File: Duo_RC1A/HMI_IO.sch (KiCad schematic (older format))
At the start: 57 parts, among them P3 CONN_2_SMD_BACKLIGHT, P4 CONN_2_SMD_BACKLIGHT, P5 PIN_ARRAY_4X1

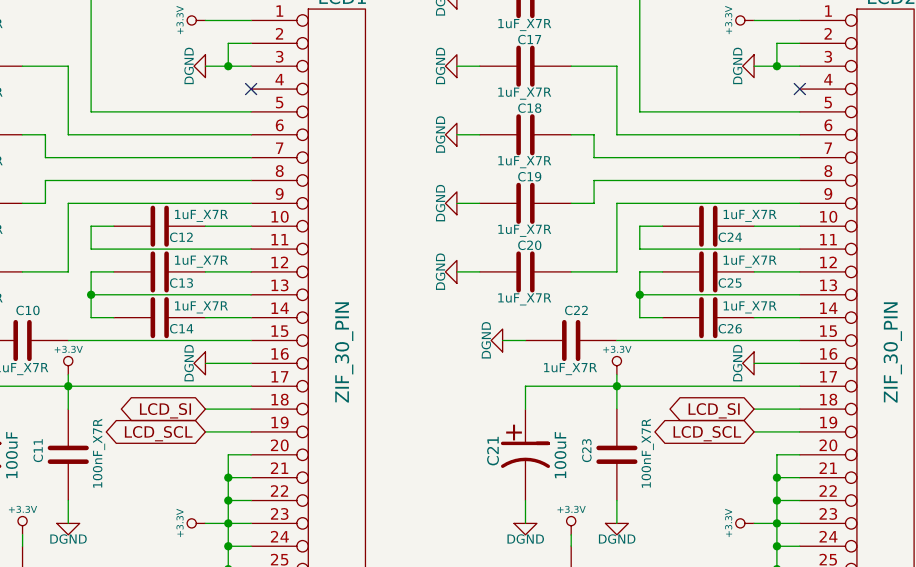
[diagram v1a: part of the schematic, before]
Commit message: Working on the BottomBoard layout. Moved the ITEAD Coreboard to the board left side so there is more space for the linear regulators. Stopped on the USB OTG and USB Host layout.
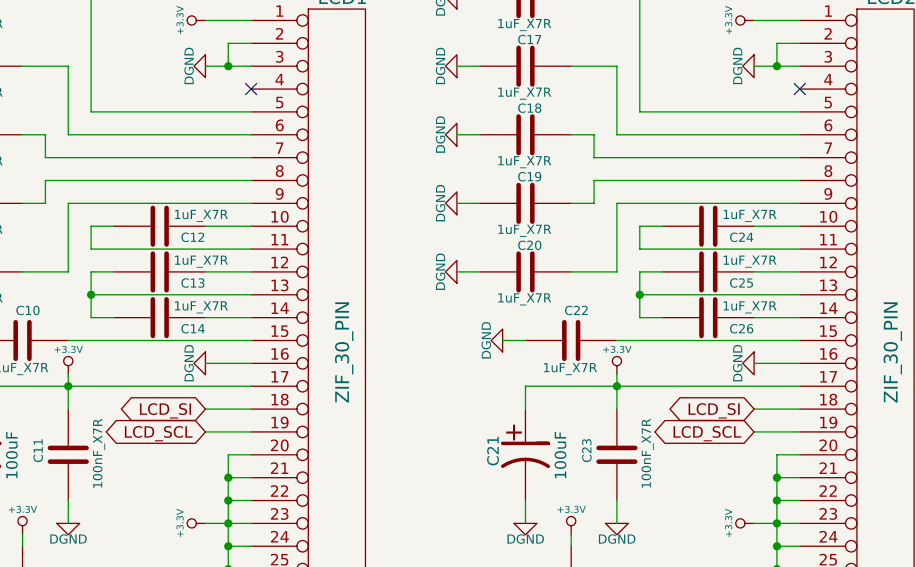
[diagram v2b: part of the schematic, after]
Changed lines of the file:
@@
 U 1 1 5371B976
 P 4900 3050
-F 0 "C26" V 4950 2900 40  0000 L CNN
+F 0 "C26" V 4950 2850 40  0000 L CNN
 F 1 "1uF_X7R" V 4850 2750 40  0000 L CNN
 F 2 "Duo_Audio_HMI_RC1A:SM0603" H 4938 2900 30  0001 C CNN
@@
 U 1 1 5371C10E
 P 4900 2850
-F 0 "C25" V 4950 2700 40  0000 L CNN
+F 0 "C25" V 4950 2650 40  0000 L CNN
 F 1 "1uF_X7R" V 4850 2550 40  0000 L CNN
 F 2 "Duo_Audio_HMI_RC1A:SM0603" H 4938 2700 30  0001 C CNN
@@
 U 1 1 5371CD0F
 P 4900 2650
-F 0 "C24" V 4950 2500 40  0000 L CNN
+F 0 "C24" V 4950 2450 40  0000 L CNN
 F 1 "1uF_X7R" V 4850 2350 40  0000 L CNN
 F 2 "Duo_Audio_HMI_RC1A:SM0603" H 4938 2500 30  0001 C CNN
@@
 U 1 1 53729A09
 P 2500 3050
-F 0 "C14" V 2550 2900 40  0000 L CNN
+F 0 "C14" V 2550 2850 40  0000 L CNN
 F 1 "1uF_X7R" V 2450 2750 40  0000 L CNN
 F 2 "Duo_Audio_HMI_RC1A:SM0603" H 2538 2900 30  0001 C CNN
@@
 U 1 1 53729A0F
 P 2500 2850
-F 0 "C13" V 2550 2700 40  0000 L CNN
+F 0 "C13" V 2550 2650 40  0000 L CNN
 F 1 "1uF_X7R" V 2450 2550 40  0000 L CNN
 F 2 "Duo_Audio_HMI_RC1A:SM0603" H 2538 2700 30  0001 C CNN
@@
 U 1 1 53729A2E
 P 2500 2650
-F 0 "C12" V 2550 2500 40  0000 L CNN
+F 0 "C12" V 2550 2450 40  0000 L CNN
 F 1 "1uF_X7R" V 2450 2350 40  0000 L CNN
 F 2 "Duo_Audio_HMI_RC1A:SM0603" H 2538 2500 30  0001 C CNN

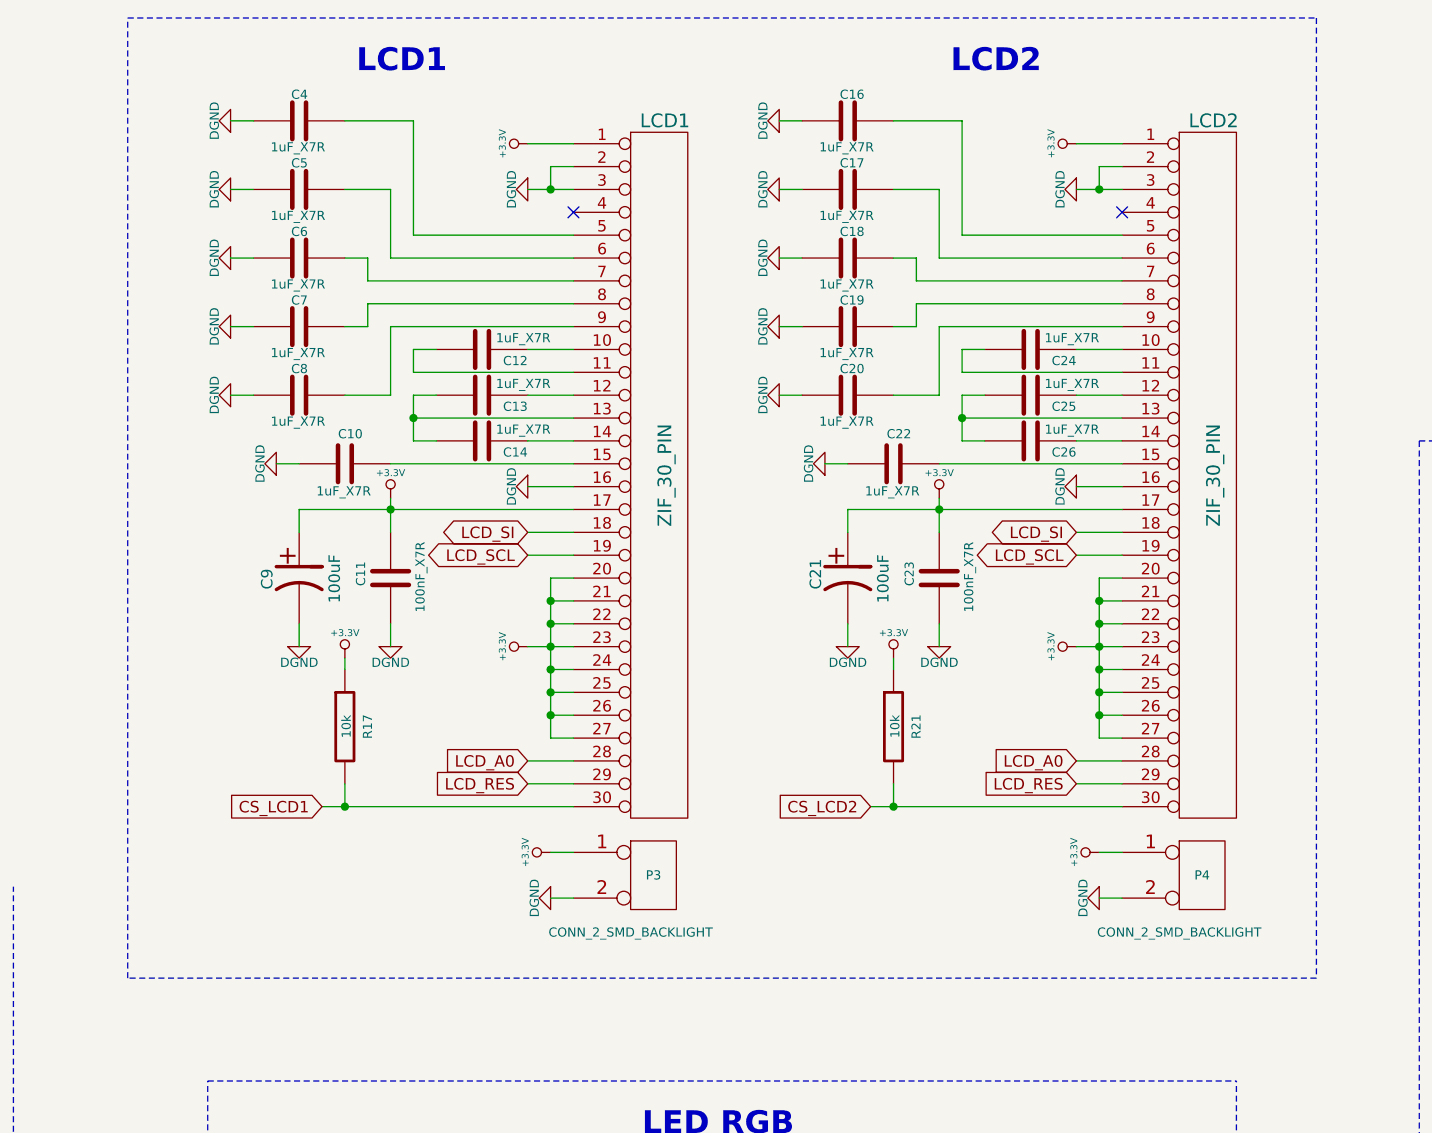
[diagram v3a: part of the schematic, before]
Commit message: Finished the TopBoard layout.
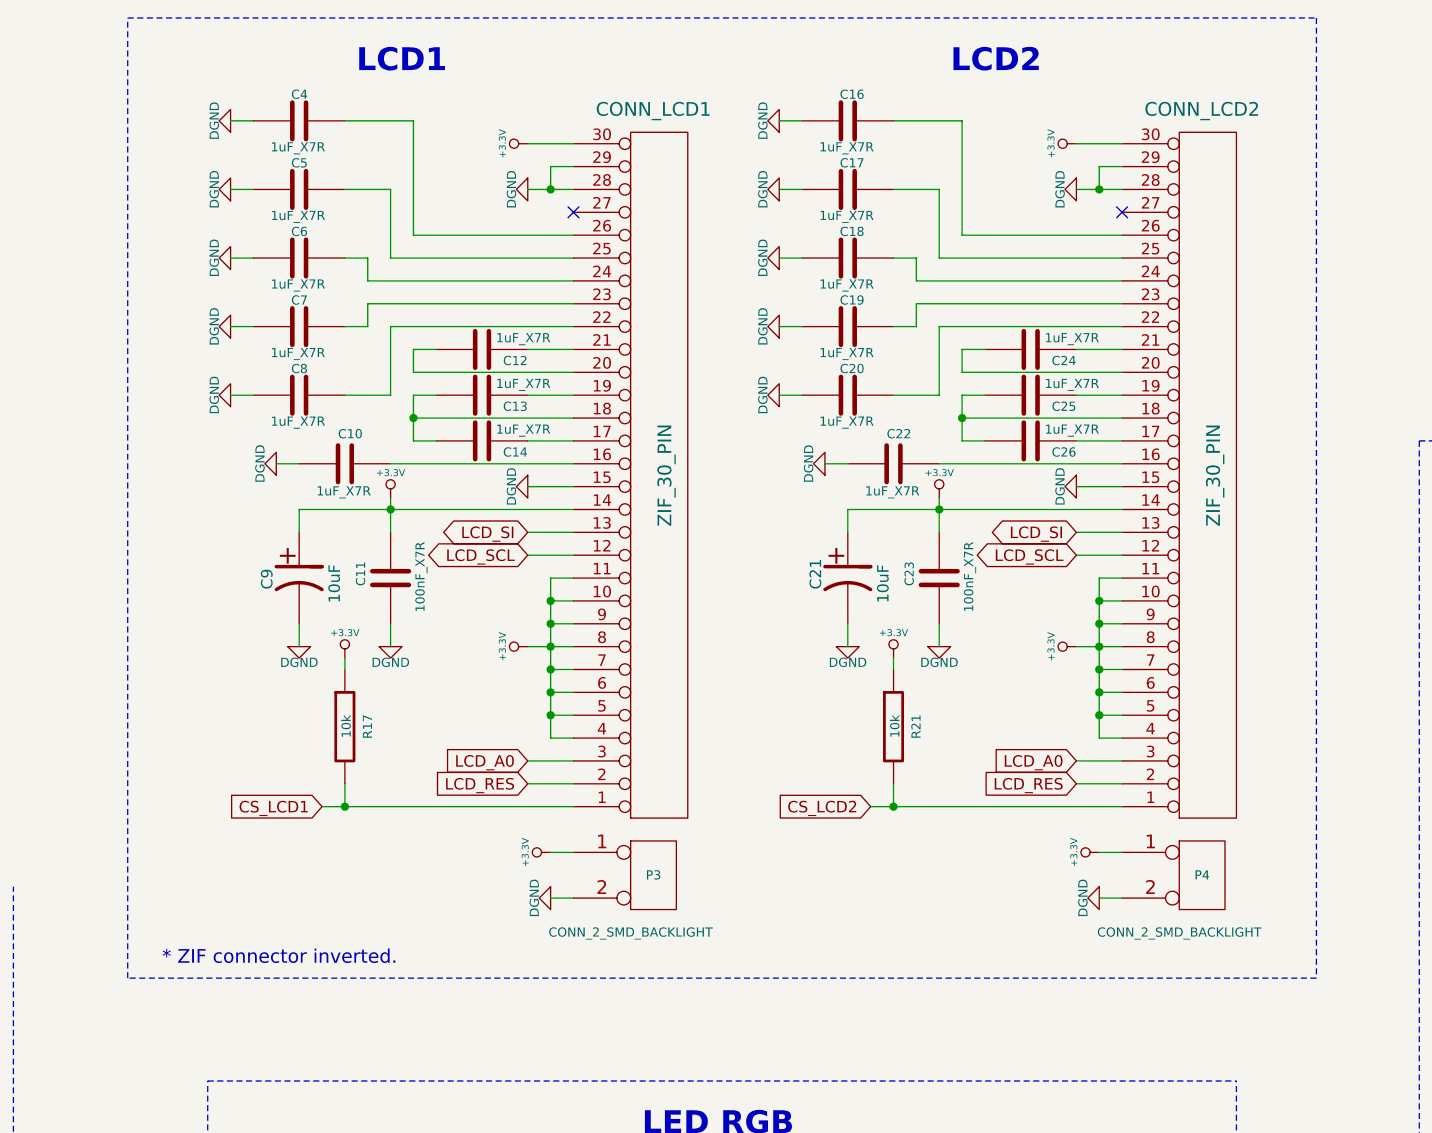
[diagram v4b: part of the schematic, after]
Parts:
- C21, C9: value 100uF -> 10uF; footprint Duo_Audio_HMI_RC1A:Capacitor5x11RM2 -> Duo_Audio_HMI_RC1A:SM0805
- renumbered LCD1 to CONN_LCD1, LCD2 to CONN_LCD2
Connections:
- net +3.3V: now also CONN_LCD1.10 (P10), CONN_LCD1.11 (P11), CONN_LCD1.14 (P14), CONN_LCD1.30 (P30), CONN_LCD1.4 (P4), CONN_LCD1.5 (P5), CONN_LCD1.6 (P6), CONN_LCD1.7 (P7), CONN_LCD1.8 (P8), CONN_LCD1.9 (P9), CONN_LCD2.10 (P10), CONN_LCD2.11 (P11), CONN_LCD2.14 (P14), CONN_LCD2.30 (P30), CONN_LCD2.4 (P4), CONN_LCD2.5 (P5), CONN_LCD2.6 (P6), CONN_LCD2.7 (P7), CONN_LCD2.8 (P8), CONN_LCD2.9 (P9); no longer CONN_LCD1.1 (P1), CONN_LCD1.17 (P17), CONN_LCD1.20 (P20), CONN_LCD1.21 (P21), CONN_LCD1.22 (P22), CONN_LCD1.23 (P23), CONN_LCD1.24 (P24), CONN_LCD1.25 (P25), CONN_LCD1.26 (P26), CONN_LCD1.27 (P27), CONN_LCD2.1 (P1), CONN_LCD2.17 (P17), CONN_LCD2.20 (P20), CONN_LCD2.21 (P21), CONN_LCD2.22 (P22), CONN_LCD2.23 (P23), CONN_LCD2.24 (P24), CONN_LCD2.25 (P25), CONN_LCD2.26 (P26), CONN_LCD2.27 (P27)
- net CS_LCD1: now also CONN_LCD1.1 (P1); no longer CONN_LCD1.30 (P30)
- net CS_LCD2: now also CONN_LCD2.1 (P1); no longer CONN_LCD2.30 (P30)
- net DGND: now also CONN_LCD1.15 (P15), CONN_LCD1.28 (P28), CONN_LCD1.29 (P29), CONN_LCD2.15 (P15), CONN_LCD2.28 (P28), CONN_LCD2.29 (P29); no longer CONN_LCD1.16 (P16), CONN_LCD1.2 (P2), CONN_LCD1.3 (P3), CONN_LCD2.16 (P16), CONN_LCD2.2 (P2), CONN_LCD2.3 (P3)
- net LCD_A0: now also CONN_LCD1.3 (P3), CONN_LCD2.3 (P3); no longer CONN_LCD1.28 (P28), CONN_LCD2.28 (P28)
- net LCD_RES: now also CONN_LCD1.2 (P2), CONN_LCD2.2 (P2); no longer CONN_LCD1.29 (P29), CONN_LCD2.29 (P29)
- net LCD_SCL: now also CONN_LCD1.12 (P12), CONN_LCD2.12 (P12); no longer CONN_LCD1.19 (P19), CONN_LCD2.19 (P19)
- net LCD_SI: now also CONN_LCD1.13 (P13), CONN_LCD2.13 (P13); no longer CONN_LCD1.18 (P18), CONN_LCD2.18 (P18)
- net at C24.2: now also CONN_LCD2.21 (P21); no longer CONN_LCD2.10 (P10)
- net at C24.1: now also CONN_LCD2.20 (P20); no longer CONN_LCD2.11 (P11)
- net at C25.2: now also CONN_LCD2.19 (P19); no longer CONN_LCD2.12 (P12)
- net at C25.1, C26.1: now also CONN_LCD2.18 (P18); no longer CONN_LCD2.13 (P13)
- net at C26.2: now also CONN_LCD2.17 (P17); no longer CONN_LCD2.14 (P14)
- net at C22.1: now also CONN_LCD2.16 (P16); no longer CONN_LCD2.15 (P15)
- net at C16.1: now also CONN_LCD2.26 (P26); no longer CONN_LCD2.5 (P5)
- net at C17.1: now also CONN_LCD2.25 (P25); no longer CONN_LCD2.6 (P6)
- net at C18.1: now also CONN_LCD2.24 (P24); no longer CONN_LCD2.7 (P7)
- net at C19.1: now also CONN_LCD2.23 (P23); no longer CONN_LCD2.8 (P8)
- net at C20.1: now also CONN_LCD2.22 (P22); no longer CONN_LCD2.9 (P9)
- net at C12.2: now also CONN_LCD1.21 (P21); no longer CONN_LCD1.10 (P10)
- net at C12.1: now also CONN_LCD1.20 (P20); no longer CONN_LCD1.11 (P11)
- net at C13.2: now also CONN_LCD1.19 (P19); no longer CONN_LCD1.12 (P12)
- net at C13.1, C14.1: now also CONN_LCD1.18 (P18); no longer CONN_LCD1.13 (P13)
- net at C14.2: now also CONN_LCD1.17 (P17); no longer CONN_LCD1.14 (P14)
- net at C10.1: now also CONN_LCD1.16 (P16); no longer CONN_LCD1.15 (P15)
- net at C4.1: now also CONN_LCD1.26 (P26); no longer CONN_LCD1.5 (P5)
- net at C5.1: now also CONN_LCD1.25 (P25); no longer CONN_LCD1.6 (P6)
- net at C6.1: now also CONN_LCD1.24 (P24); no longer CONN_LCD1.7 (P7)
- net at C7.1: now also CONN_LCD1.23 (P23); no longer CONN_LCD1.8 (P8)
- net at C8.1: now also CONN_LCD1.22 (P22); no longer CONN_LCD1.9 (P9)
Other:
- note added: "* ZIF connector inverted."

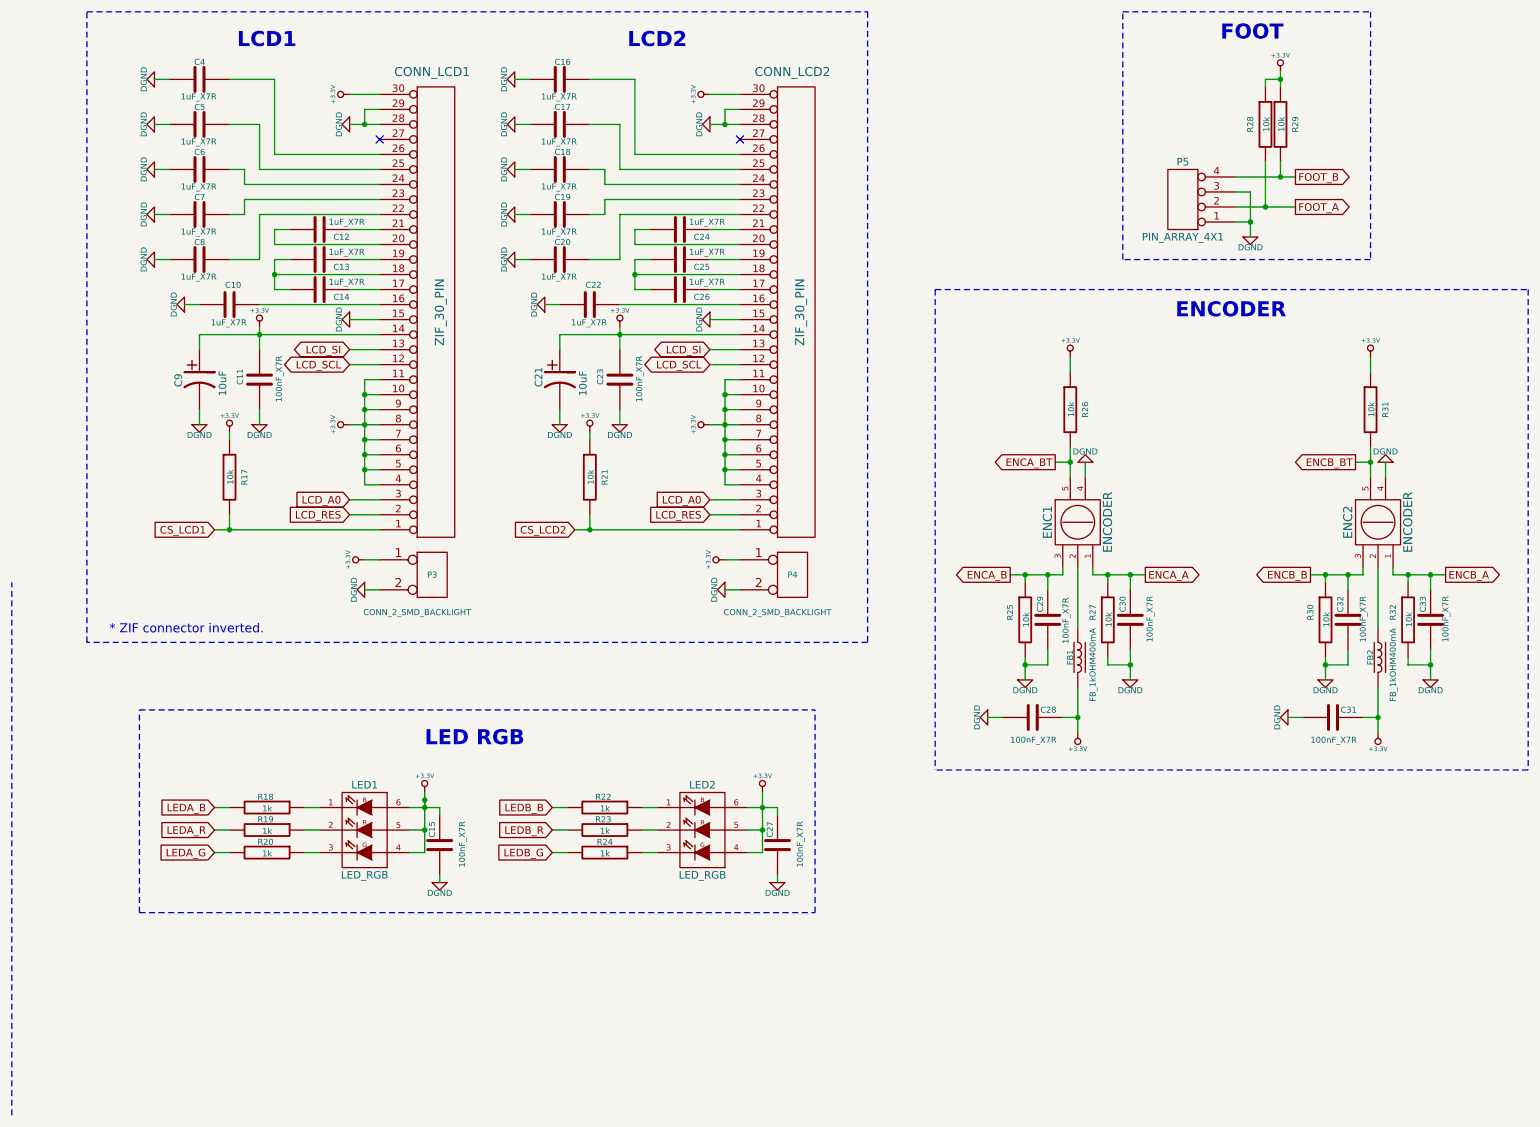
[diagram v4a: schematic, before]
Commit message: Removed some of the audio CODEC signals for Minimal Viable Product. Need to change the 3.3V regulator to the Top Board.
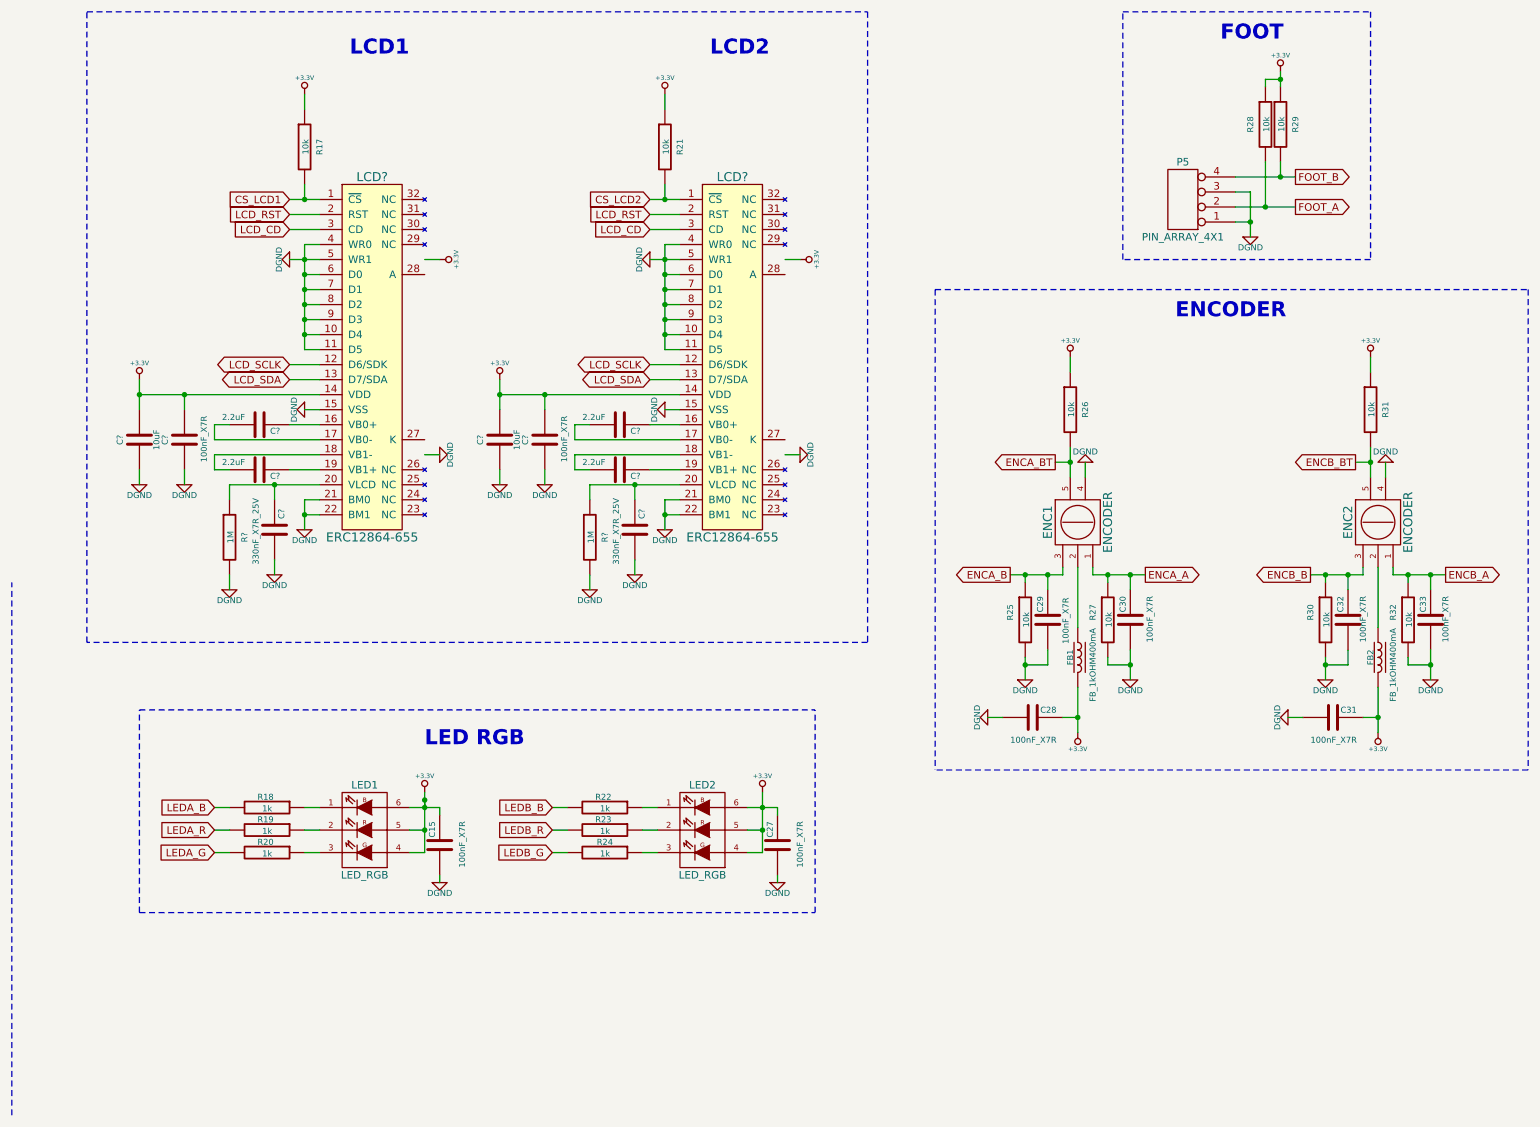
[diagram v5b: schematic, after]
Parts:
- removed C10, C12, C13, C14, C16, C17, C18, C19, C20, C22, C24, C25, C26, C4, C5, C6, C7, C8: 1uF_X7R, Duo_Audio_HMI_RC1A:SM0603, symbol C
- removed C11, C23: 100nF_X7R, Duo_Audio_HMI_RC1A:SM0603, symbol C
- removed C21, C9: 10uF, Duo_Audio_HMI_RC1A:SM0805, symbol CP1
- removed CONN_LCD1, CONN_LCD2: ZIF_30_PIN, Duo_Audio_HMI_RC1A:ER_CON30HB_1, symbol CONN_30
- removed P3, P4: CONN_2_SMD_BACKLIGHT, Duo_Audio_HMI_RC1A:ER_CON2.0_2P_SMD, symbol CONN_2
- added C? (x2): 100nF_X7R, Duo_Audio_HMI_RC1A:SM0603, symbol C
- added C? (x2): 10uF, Duo_Audio_HMI_RC1A:SM0805, symbol C
- added C? (x2): 330nF_X7R_25V, Duo_Audio_HMI_RC1A:SM0603, symbol C
- added C? (x4): 2.2uF, Duo_Audio_HMI_RC1A:SM0603, symbol C
- added LCD? (x2): ERC12864-655, symbol ERC12864-655
- added R? (x2): 1M, Duo_Audio_HMI_RC1A:SM0603, symbol R
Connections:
- net +3.3V: now also C?.1, C?.1, C?.1, C?.1, LCD?.14 (VDD), LCD?.14 (VDD)
- net CS_LCD1: now also LCD?.1 (~CS)
- net CS_LCD2: now also LCD?.1 (~CS)
- net DGND: now also C?.2, C?.2, C?.2, C?.2, C?.2, C?.2, LCD?.10 (D4), LCD?.10 (D4), LCD?.11 (D5), LCD?.11 (D5), LCD?.15 (VSS), LCD?.15 (VSS), LCD?.21 (BM0), LCD?.21 (BM0), LCD?.22 (BM1), LCD?.22 (BM1), LCD?.4 (WR0), LCD?.4 (WR0), LCD?.5 (WR1), LCD?.5 (WR1), LCD?.6 (D0), LCD?.6 (D0), LCD?.7 (D1), LCD?.7 (D1), LCD?.8 (D2), LCD?.8 (D2), LCD?.9 (D3), LCD?.9 (D3), R?.2, R?.2
- new net: C?.1, LCD?.16 (VB0+) (x2)
- new net: C?.2, LCD?.17 (VB0-) (x2)
- new net: C?.2, LCD?.18 (VB1-) (x2)
- new net: C?.1, LCD?.19 (VB1+) (x2)
- new net: C?.1, LCD?.20 (VLCD), R?.1 (x2)
- new net LCD_CD: LCD?.3 (CD), LCD?.3 (CD)
- new net LCD_RST: LCD?.2 (RST), LCD?.2 (RST)
- new net LCD_SCLK: LCD?.12 (D6/SDK), LCD?.12 (D6/SDK)
- new net LCD_SDA: LCD?.13 (D7/SDA), LCD?.13 (D7/SDA)
- no-connect marks 2 -> 0
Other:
- note removed: "* ZIF connector inverted."
- moved on the sheet: R17, R21
